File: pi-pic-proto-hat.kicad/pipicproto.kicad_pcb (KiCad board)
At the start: 2 copper layers, 65 x 56 mm, 23 parts, among them J1 RUN/~PGM~, J10 Conn_01x13_Male, J2 Conn_01x02_Male, J22 Conn_01x13_Male, J3 Conn_01x02_Male, J6 Barrel_Jack_Switch, J7 Conn_01x20_Male, J8 Conn_01x06_Male, J9 Conn_01x02_Male, P1 Conn_02x20_Odd_Even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

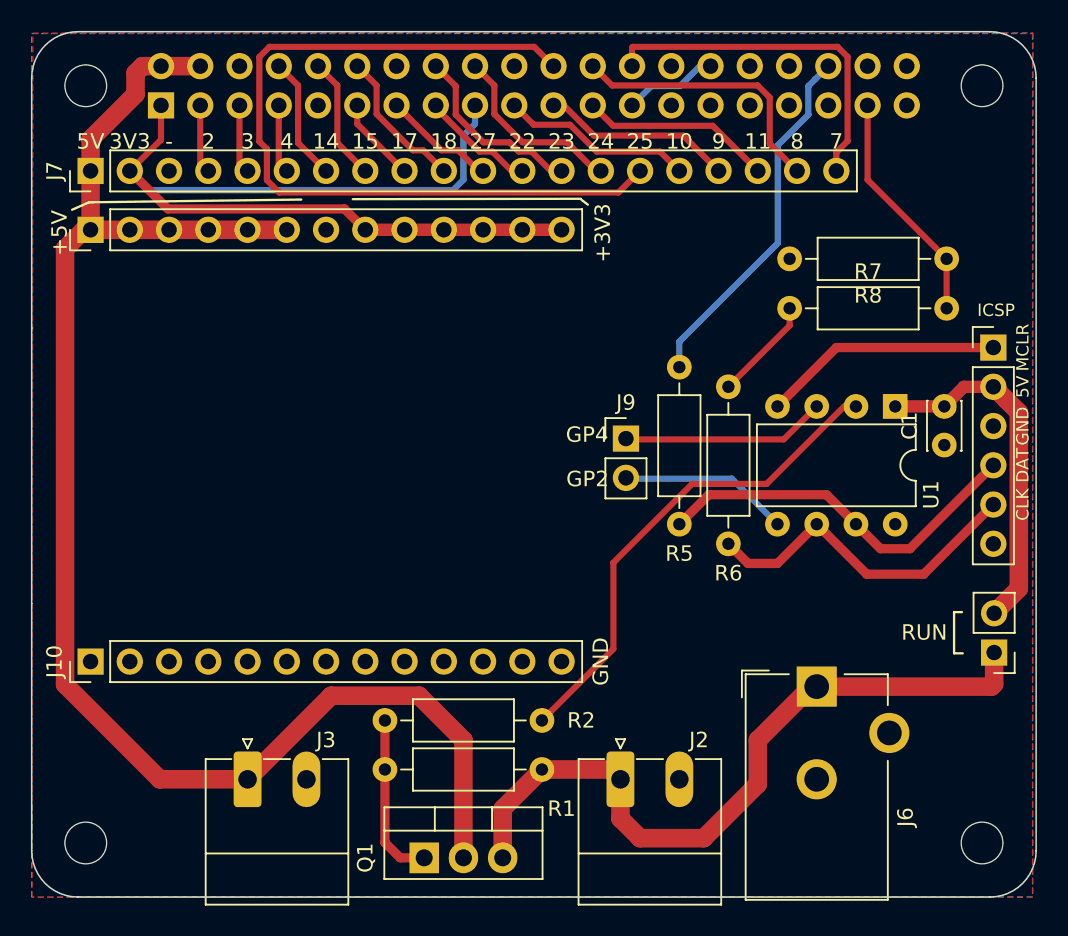
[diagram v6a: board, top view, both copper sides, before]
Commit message: V2.06: remove R6 (not needed, since we added a voltage-divider)
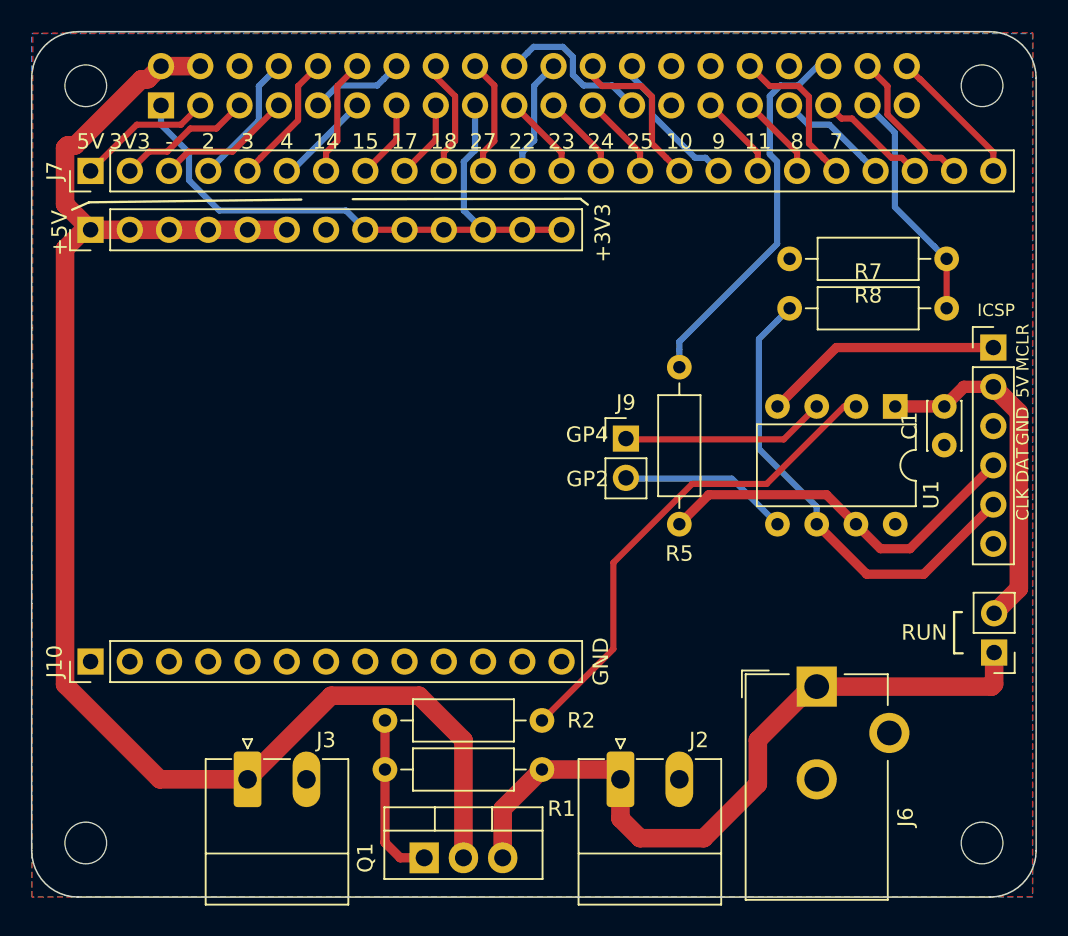
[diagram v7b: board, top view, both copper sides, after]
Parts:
- removed R6: 1k, Resistor_THT:R_Axial_DIN0207_L6.3mm_D2.5mm_P10.16mm_Horizontal
- J7: value Conn_01x20_Male -> Conn_01x24_Male; footprint Connector_PinHeader_2.54mm:PinHeader_1x20_P2.54mm_Vertical -> Connector_PinHeader_2.54mm:PinHeader_1x24_P2.54mm_Vertical
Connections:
- J7 pad 1: +5V -> /GPIO2(SDA1)
- J7 pad 10: /GPIO18(GEN1)(PWM0) -> /GPIO23(GEN4)
- J7 pad 11: /GPIO27(GEN2) -> /GPIO24(GEN5)
- J7 pad 12: /GPIO22(GEN3) -> /GPIO25(GEN6)
- J7 pad 13: /GPIO23(GEN4) -> /GPIO10(SPI0_MOSI)
- J7 pad 14: /GPIO24(GEN5) -> /GPIO9(SPI0_MISO)
- J7 pad 15: /GPIO25(GEN6) -> /GPIO11(SPI0_SCK)
- J7 pad 16: /GPIO10(SPI0_MOSI) -> /GPIO8(SPI0_CE_0)
- J7 pad 17: /GPIO9(SPI0_MISO) -> /GPIO7(SPI0_CE_1)
- J7 pad 18: /GPIO11(SPI0_SCK) -> /GPIO5
- J7 pad 19: /GPIO8(SPI0_CE_0) -> /GPIO6
- J7 pad 2: +3V3 -> /GPIO3(SCL1)
- J7 pad 20: /GPIO7(SPI0_CE_1) -> /GPIO12(PWM0)
- J7 pad 3: GND -> /GPIO4(GCLK)
- J7 pad 4: /GPIO2(SDA1) -> /GPIO14(TXD0)
- J7 pad 5: /GPIO3(SCL1) -> /GPIO15(RXD0)
- J7 pad 6: /GPIO4(GCLK) -> /GPIO17(GEN0)
- J7 pad 7: /GPIO14(TXD0) -> /GPIO18(GEN1)(PWM0)
- J7 pad 8: /GPIO15(RXD0) -> /GPIO27(GEN2)
- J7 pad 9: /GPIO17(GEN0) -> /GPIO22(GEN3)
- R7 pad 1: Net-(R6-Pad2) -> /CLK
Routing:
- net /GPIO25(GEN6): track 53.1 -> 7.62 mm
- net +3V3: track 62.7 -> 39.9 mm
- net /GPIO7(SPI0_CE_1): track 23.1 -> 9.49 mm
- net GND: track 6.13 -> 16.5 mm
- net /GPIO12(PWM0): track 0.00 -> 10.2 mm
- net /GPIO20(SPI1_MOSI): track 0.00 -> 9.49 mm
- net /GPIO21(SPI1_SCK): track 0.00 -> 9.11 mm
- net /CLK: track 21.9 -> 31.0 mm
- net /GPIO13(PWM1): track 0.00 -> 7.36 mm
- net /GPIO19(SPI1_MISO): track 0.00 -> 7.36 mm
- net /GPIO8(SPI0_CE_0): track 17.8 -> 10.6 mm
- net /GPIO10(SPI0_MOSI): track 12.4 -> 5.51 mm
- net /GPIO11(SPI0_SCK): track 12.4 -> 5.51 mm
- net Net-(R6-Pad2): track 6.72 -> 0.00 mm
- net /GPIO9(SPI0_MISO): track 12.4 -> 6.17 mm
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
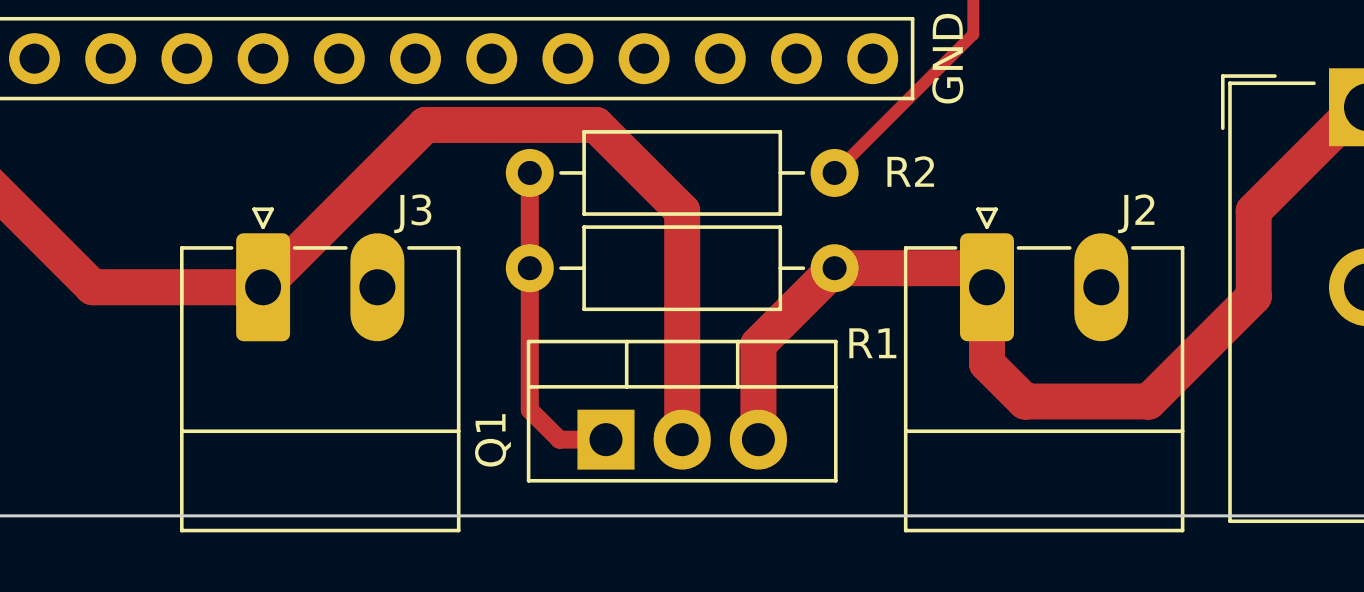
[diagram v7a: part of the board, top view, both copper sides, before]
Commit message: V2.07: remove J2/J3 connectors
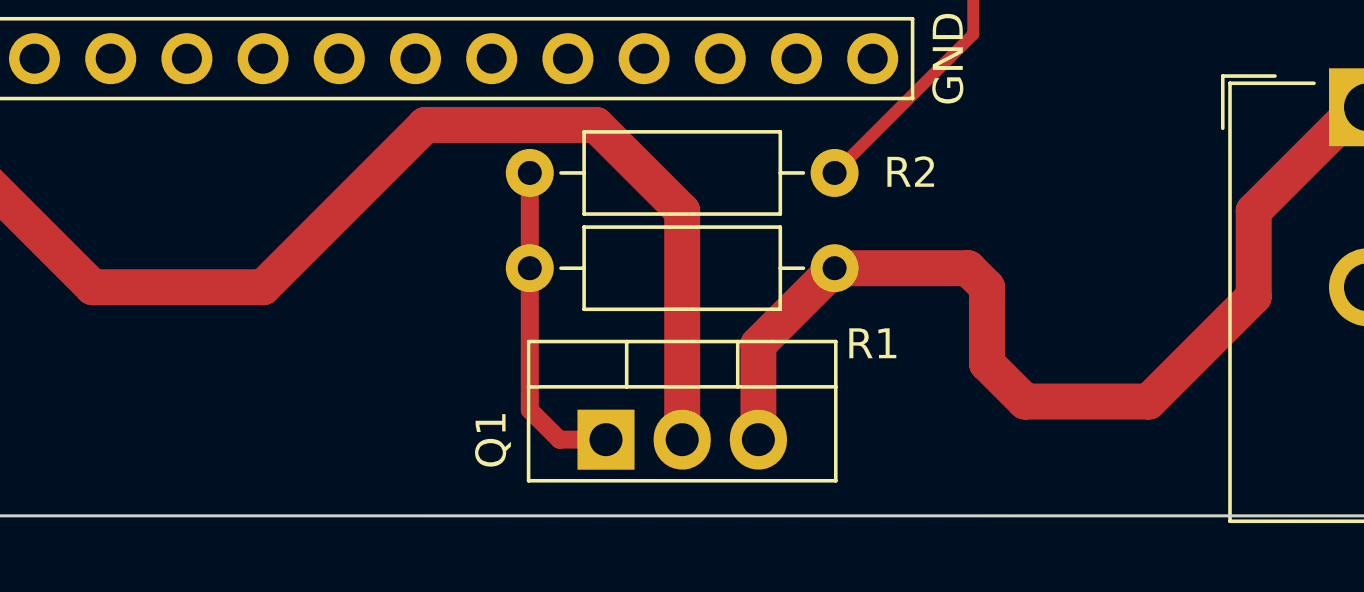
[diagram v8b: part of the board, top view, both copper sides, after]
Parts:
- removed J2, J3: Conn_01x02_Male, Connector_Phoenix_MC:PhoenixContact_MC_1,5_2-G-3.81_1x02_P3.81mm_Horizontal
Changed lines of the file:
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@@
     (tracks 195)
     (zones 0)
-    (modules 22)
+    (modules 20)
     (nets 44)
   )
@@
       (at (xyz 0 0 0))
       (scale (xyz 1 1 1))
-      (rotate (xyz 0 0 0))
-    )
-  )
-  (module Connector_Phoenix_MC:PhoenixContact_MC_1,5_2-G-3.81_1x02_P3.81mm_Horizontal (layer F.Cu)
-    (at 238.1 142.38)
-    (descr "Generic Phoenix Contact connector footprint for: MC_1,5/2-G-3.81; number of pins: 02; pin pitch: 3.81mm; Angled || order number: 1803277 8A 160V")
-    (tags "phoenix_contact connector MC_01x02_G_3.81mm")
-    (fp_text reference J2 (at 5.08 -2.54) (layer F.SilkS)
-      (effects (font (size 1 1) (thickness 0.15)))
-    )
-    (fp_text value Conn_01x02_Male (at 1.9 9.2) (layer F.Fab)
-      (effects (font (size 1 1) (thickness 0.15)))
-    )
-    (fp_text user %R (at 1.9 -0.5) (layer F.Fab)
-      (effects (font (size 1 1) (thickness 0.15)))
-    )
-    (fp_line (start 0 0) (end -0.8 -1.2) (layer F.Fab) (width 0.1))
-    (fp_line (start 0.8 -1.2) (end 0 0) (layer F.Fab) (width 0.1))
-    (fp_line (start -0.3 -2.6) (end 0.3 -2.6) (layer F.SilkS) (width 0.12))
-    (fp_line (start 0 -2) (end -0.3 -2.6) (layer F.SilkS) (width 0.12))
-    (fp_line (start 0.3 -2.6) (end 0 -2) (layer F.SilkS) (width 0.12))
-    (fp_line (start 6.91 -2.3) (end -3.21 -2.3) (layer F.CrtYd) (width 0.05))
-    (fp_line (start 6.91 8.5) (end 6.91 -2.3) (layer F.CrtYd) (width 0.05))
-    (fp_line (start -3.21 8.5) (end 6.91 8.5) (layer F.CrtYd) (width 0.05))
-    (fp_line (start -3.21 -2.3) (end -3.21 8.5) (layer F.CrtYd) (width 0.05))
-    (fp_line (start -2.71 4.8) (end 6.52 4.8) (layer F.SilkS) (width 0.12))
-    (fp_line (start 6.41 -1.2) (end -2.6 -1.2) (layer F.Fab) (width 0.1))
-    (fp_line (start 6.41 8) (end 6.41 -1.2) (layer F.Fab) (width 0.1))
-    (fp_line (start -2.6 8) (end 6.41 8) (layer F.Fab) (width 0.1))
-    (fp_line (start -2.6 -1.2) (end -2.6 8) (layer F.Fab) (width 0.1))
-    (fp_line (start 1.05 -1.31) (end 2.76 -1.31) (layer F.SilkS) (width 0.12))
-    (fp_line (start 6.52 -1.31) (end 4.86 -1.31) (layer F.SilkS) (width 0.12))
-    (fp_line (start -2.71 -1.31) (end -1.05 -1.31) (layer F.SilkS) (width 0.12))
-    (fp_line (start 6.52 8.11) (end 6.52 -1.31) (layer F.SilkS) (width 0.12))
-    (fp_line (start -2.71 8.11) (end 6.52 8.11) (layer F.SilkS) (width 0.12))
-    (fp_line (start -2.71 -1.31) (end -2.71 8.11) (layer F.SilkS) (width 0.12))
-    (pad 2 thru_hole oval (at 3.81 0) (size 1.8 3.6) (drill 1.2) (layers *.Cu *.Mask)
-      (net 3 GND))
-    (pad 1 thru_hole roundrect (at 0 0) (size 1.8 3.6) (drill 1.2) (layers *.Cu *.Mask) (roundrect_rratio 0.138889)
-      (net 43 +5P))
-    (model ${KISYS3DMOD}/Connector_Phoenix_MC.3dshapes/PhoenixContact_MC_1,5_2-G-3.81_1x02_P3.81mm_Horizontal.wrl
-      (at (xyz 0 0 0))
-      (scale (xyz 1 1 1))
-      (rotate (xyz 0 0 0))
-    )
-  )
-  (module Connector_Phoenix_MC:PhoenixContact_MC_1,5_2-G-3.81_1x02_P3.81mm_Horizontal (layer F.Cu)
-    (at 213.97 142.38)
-    (descr "Generic Phoenix Contact connector footprint for: MC_1,5/2-G-3.81; number of pins: 02; pin pitch: 3.81mm; Angled || order number: 1803277 8A 160V")
-    (tags "phoenix_contact connector MC_01x02_G_3.81mm")
-    (fp_text reference J3 (at 5.08 -2.54) (layer F.SilkS)
-      (effects (font (size 1 1) (thickness 0.15)))
-    )
-    (fp_text value Conn_01x02_Male (at 1.9 9.2) (layer F.Fab)
-      (effects (font (size 1 1) (thickness 0.15)))
-    )
-    (fp_line (start -2.71 -1.31) (end -2.71 8.11) (layer F.SilkS) (width 0.12))
-    (fp_line (start -2.71 8.11) (end 6.52 8.11) (layer F.SilkS) (width 0.12))
-    (fp_line (start 6.52 8.11) (end 6.52 -1.31) (layer F.SilkS) (width 0.12))
-    (fp_line (start -2.71 -1.31) (end -1.05 -1.31) (layer F.SilkS) (width 0.12))
-    (fp_line (start 6.52 -1.31) (end 4.86 -1.31) (layer F.SilkS) (width 0.12))
-    (fp_line (start 1.05 -1.31) (end 2.76 -1.31) (layer F.SilkS) (width 0.12))
-    (fp_line (start -2.6 -1.2) (end -2.6 8) (layer F.Fab) (width 0.1))
-    (fp_line (start -2.6 8) (end 6.41 8) (layer F.Fab) (width 0.1))
-    (fp_line (start 6.41 8) (end 6.41 -1.2) (layer F.Fab) (width 0.1))
-    (fp_line (start 6.41 -1.2) (end -2.6 -1.2) (layer F.Fab) (width 0.1))
-    (fp_line (start -2.71 4.8) (end 6.52 4.8) (layer F.SilkS) (width 0.12))
-    (fp_line (start -3.21 -2.3) (end -3.21 8.5) (layer F.CrtYd) (width 0.05))
-    (fp_line (start -3.21 8.5) (end 6.91 8.5) (layer F.CrtYd) (width 0.05))
-    (fp_line (start 6.91 8.5) (end 6.91 -2.3) (layer F.CrtYd) (width 0.05))
-    (fp_line (start 6.91 -2.3) (end -3.21 -2.3) (layer F.CrtYd) (width 0.05))
-    (fp_line (start 0.3 -2.6) (end 0 -2) (layer F.SilkS) (width 0.12))
-    (fp_line (start 0 -2) (end -0.3 -2.6) (layer F.SilkS) (width 0.12))
-    (fp_line (start -0.3 -2.6) (end 0.3 -2.6) (layer F.SilkS) (width 0.12))
-    (fp_line (start 0.8 -1.2) (end 0 0) (layer F.Fab) (width 0.1))
-    (fp_line (start 0 0) (end -0.8 -1.2) (layer F.Fab) (width 0.1))
-    (fp_text user %R (at 1.9 -0.5) (layer F.Fab)
-      (effects (font (size 1 1) (thickness 0.15)))
-    )
-    (pad 1 thru_hole roundrect (at 0 0) (size 1.8 3.6) (drill 1.2) (layers *.Cu *.Mask) (roundrect_rratio 0.138889)
-      (net 2 +5V))
-    (pad 2 thru_hole oval (at 3.81 0) (size 1.8 3.6) (drill 1.2) (layers *.Cu *.Mask)
-      (net 3 GND))
-    (model ${KISYS3DMOD}/Connector_Phoenix_MC.3dshapes/PhoenixContact_MC_1,5_2-G-3.81_1x02_P3.81mm_Horizontal.wrl
-      (at (xyz 0 0 0))
-      (scale (xyz 1 1 1))
